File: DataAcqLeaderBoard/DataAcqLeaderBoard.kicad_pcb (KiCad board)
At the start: 2 copper layers, 1 part, among them U1 PA1616S_GPS

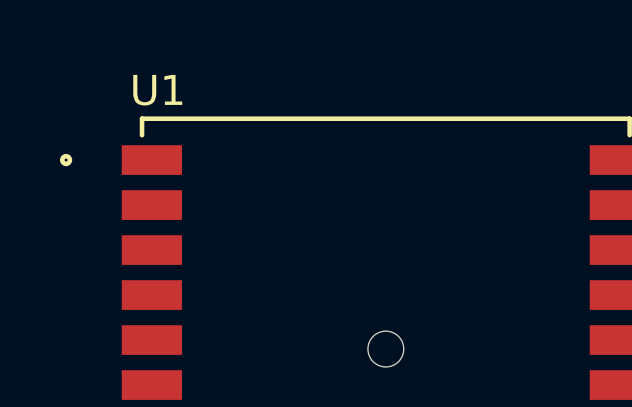
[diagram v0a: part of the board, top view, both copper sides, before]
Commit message: Removed old junk (symbol, footprint file setup)
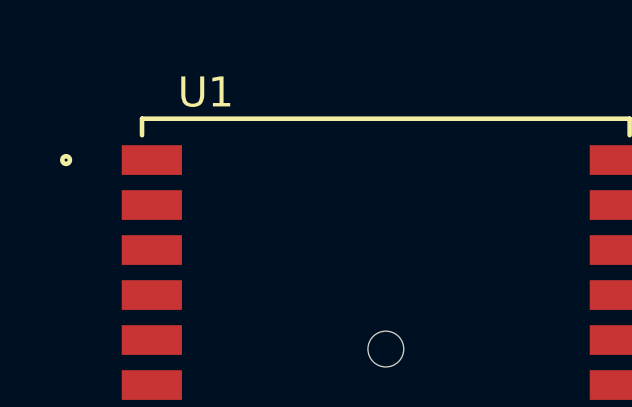
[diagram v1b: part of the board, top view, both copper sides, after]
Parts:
- U1: footprint PA_1616S_GPS:PA1616S_ADA -> DataAcqLeaderBoard-Footprints:PA1616S_ADA
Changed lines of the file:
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@@
 	(net 16 "/GPS_CoinBattery_Supply")
 	(net 17 "/GPS_NReset")
-	(footprint "PA_1616S_GPS:PA1616S_ADA"
+	(footprint "DataAcqLeaderBoard-Footprints:PA1616S_ADA"
 		(layer "F.Cu")
 		(at 175.8 93.15)
 		(tags "790 ")
 		(property "Reference" "U1"
-			(at -7.6 -9.05 0)
+			(at -6 -9 0)
 			(unlocked yes)
 			(layer "F.SilkS")
@@
 		)
 		(property "Value" "PA1616S_GPS"
-			(at 0 -5.95 0)
+			(at 0 -11 0)
 			(unlocked yes)
 			(layer "F.Fab")
@@
 			)
 		)
-		(property "Footprint" "PA_1616S_GPS:PA1616S_ADA"
+		(property "Footprint" "DataAcqLeaderBoard-Footprints:PA1616S_ADA"
 			(at 0 0 0)
 			(unlocked yes)
@@
 		)
 		(fp_text user "${REFERENCE}"
-			(at -7.6 -9.05 0)
-			(unlocked yes)
-			(layer "F.Fab")
+			(at 0 -0.5 0)
+			(unlocked yes)
+			(layer "F.Fab")

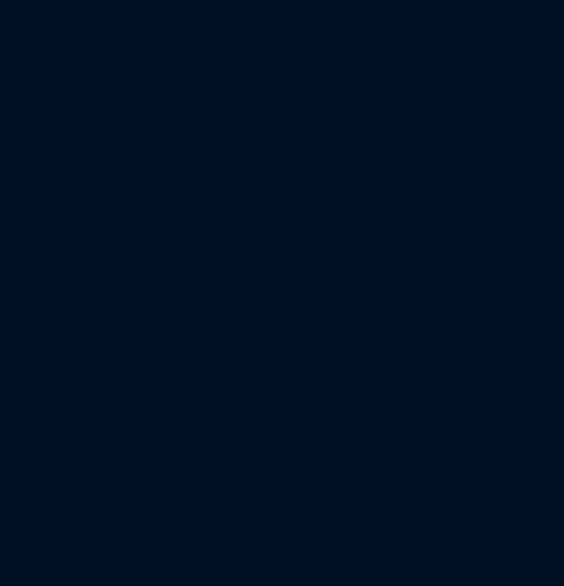
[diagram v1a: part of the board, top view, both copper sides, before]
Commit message: Added Digi XBee LTE Module
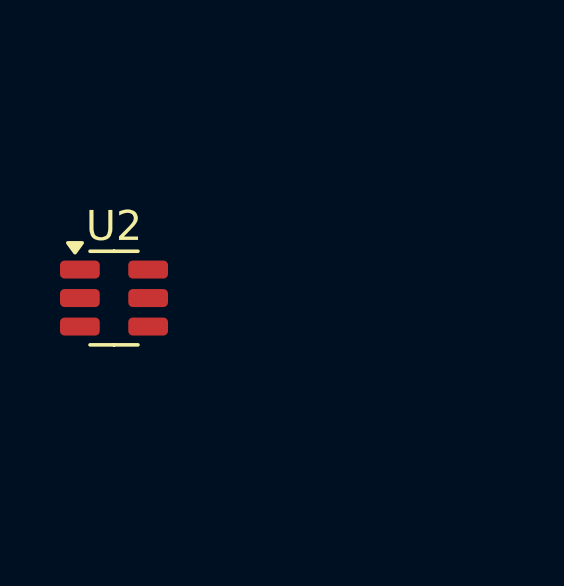
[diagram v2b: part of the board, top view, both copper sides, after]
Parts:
- added U2: USBLC6-2SC6, Package_TO_SOT_SMD:SOT-23-6, F.Cu at (147.0, 91.0)

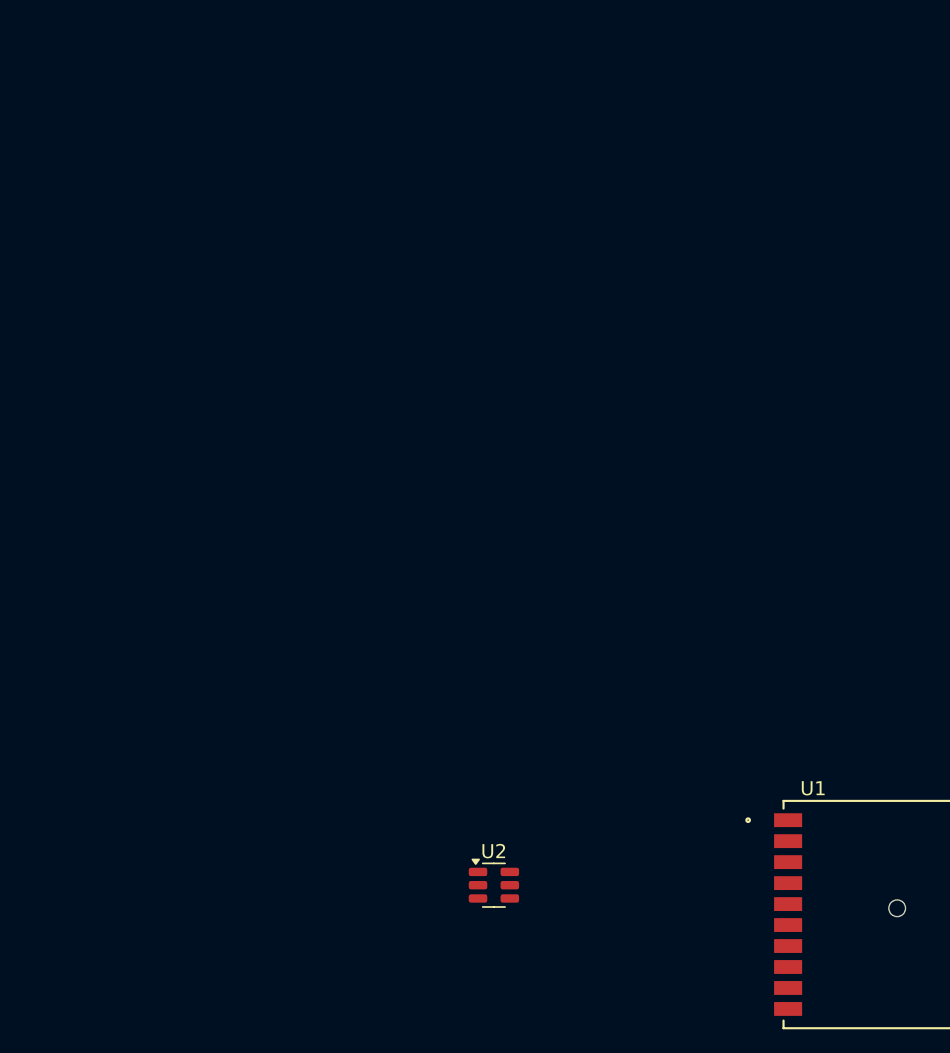
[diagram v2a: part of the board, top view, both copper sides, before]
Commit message: Added XBee RF and LTE Footprints
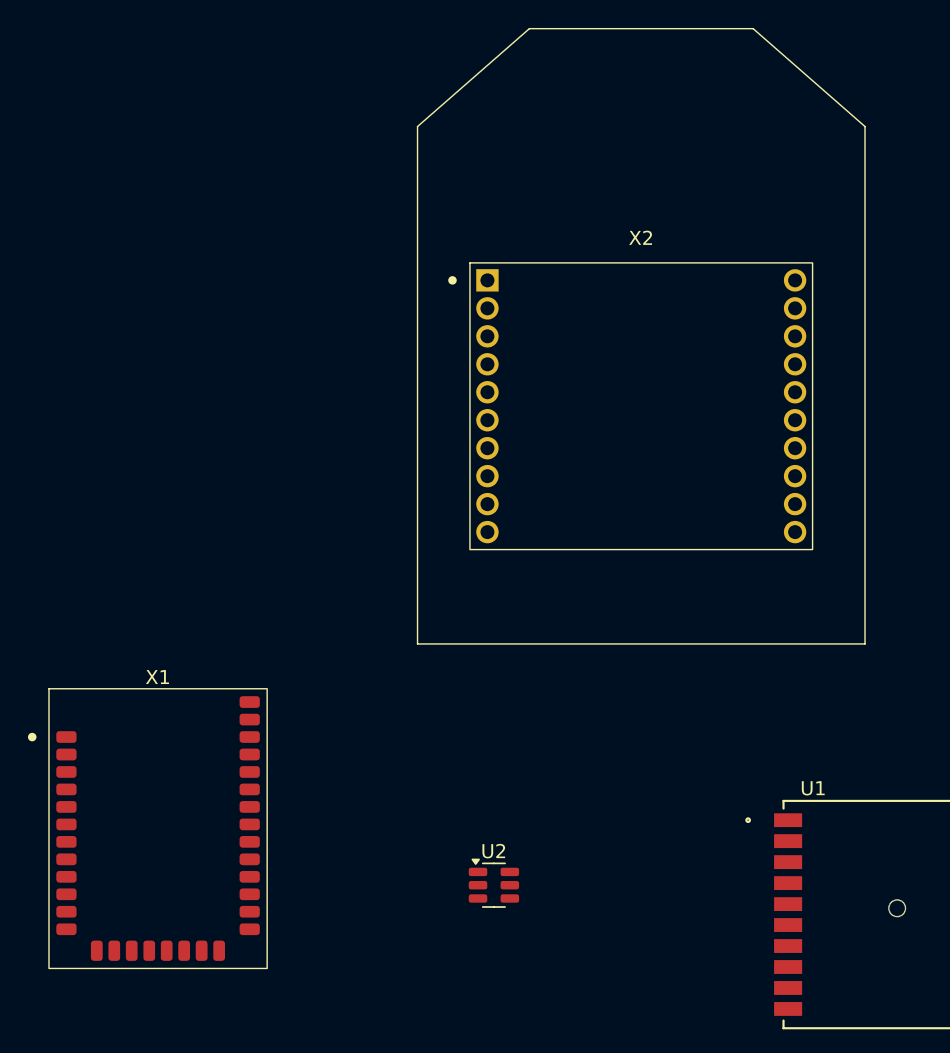
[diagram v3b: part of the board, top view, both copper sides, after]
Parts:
- added X1: DigiXBeeRX900Micro, DataAcqLeaderBoard-Footprints:XBeeXR900RFMicro, F.Cu at (122.9, 87.0)
- added X2: DigiXBee3LTECat4, DataAcqLeaderBoard-Footprints:DigiXBee3LTECat4, F.Cu at (157.5, 55.8)
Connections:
- net /GPS_1PPS_ToMCU renamed /GPS_1PPS
- net /GPS_NReset renamed /GPS_NRESET
- net Net-(U1-VCC) renamed /GPS_VCC
- U1 pad 10: /GPS_UART_RX -> unconnected-(U1-RX0-Pad10)
- U1 pad 14: unconnected-(U1-RTCM(I2C_SCL)-Pad14) -> /GPS_I2C_SCL
- U1 pad 15: unconnected-(U1-TX1(I2C_SDA)-Pad15) -> /GPS_I2C_SDA
- U1 pad 9: /GPS_UART_TX -> unconnected-(U1-TX0-Pad9)
- U2 pad 1: Net-(J2-D--PadA7) -> /USBC_D-
- U2 pad 3: Net-(J2-D+-PadA6) -> /USBC_D-

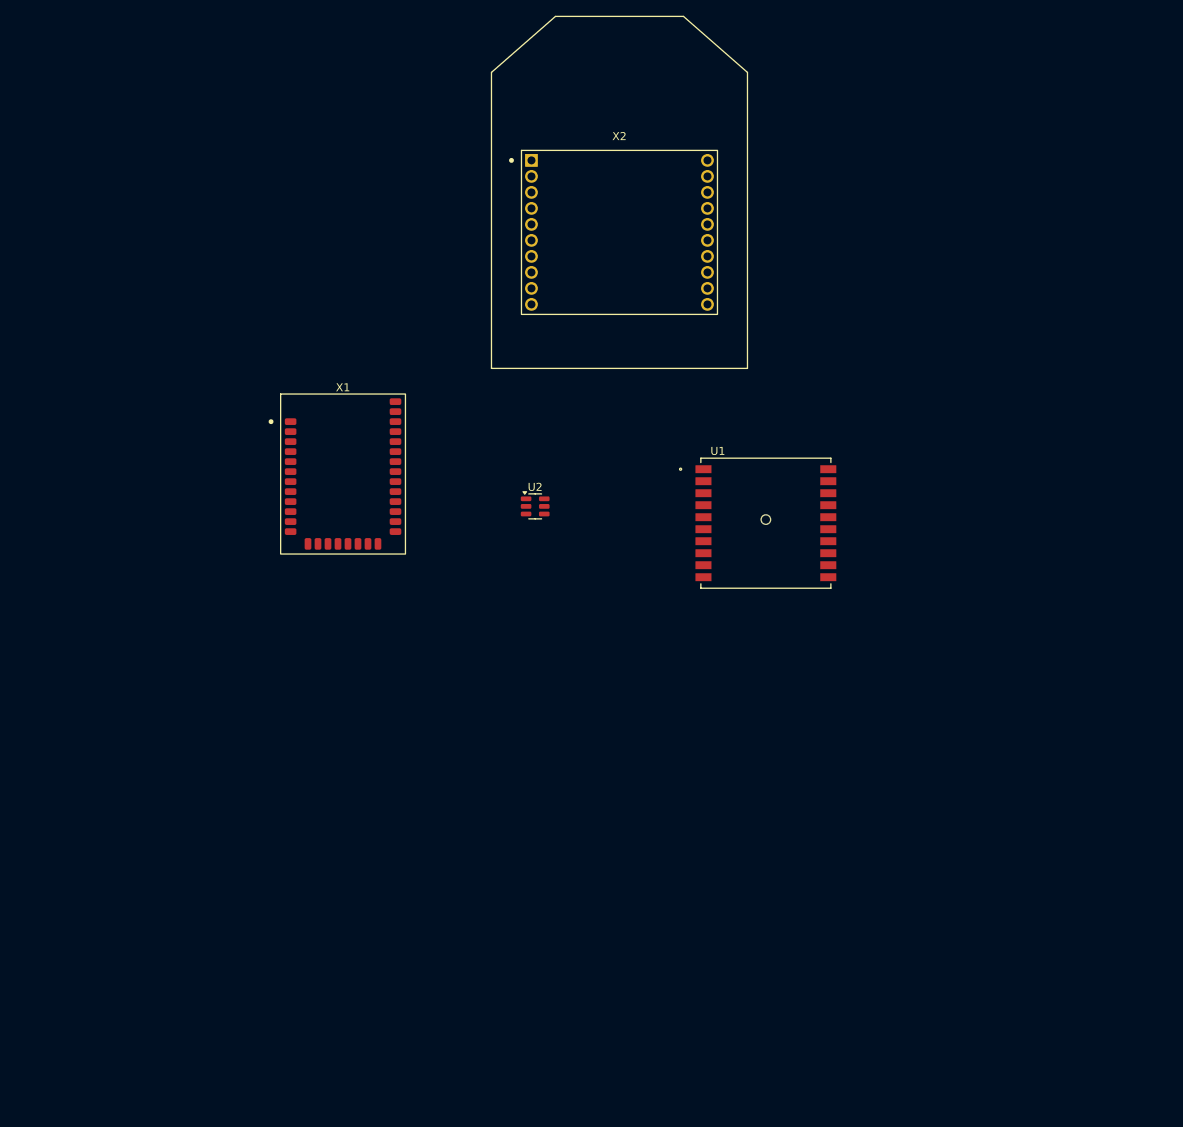
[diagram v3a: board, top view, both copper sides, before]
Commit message: Interfaced Leader SOM and added UTSVT Library
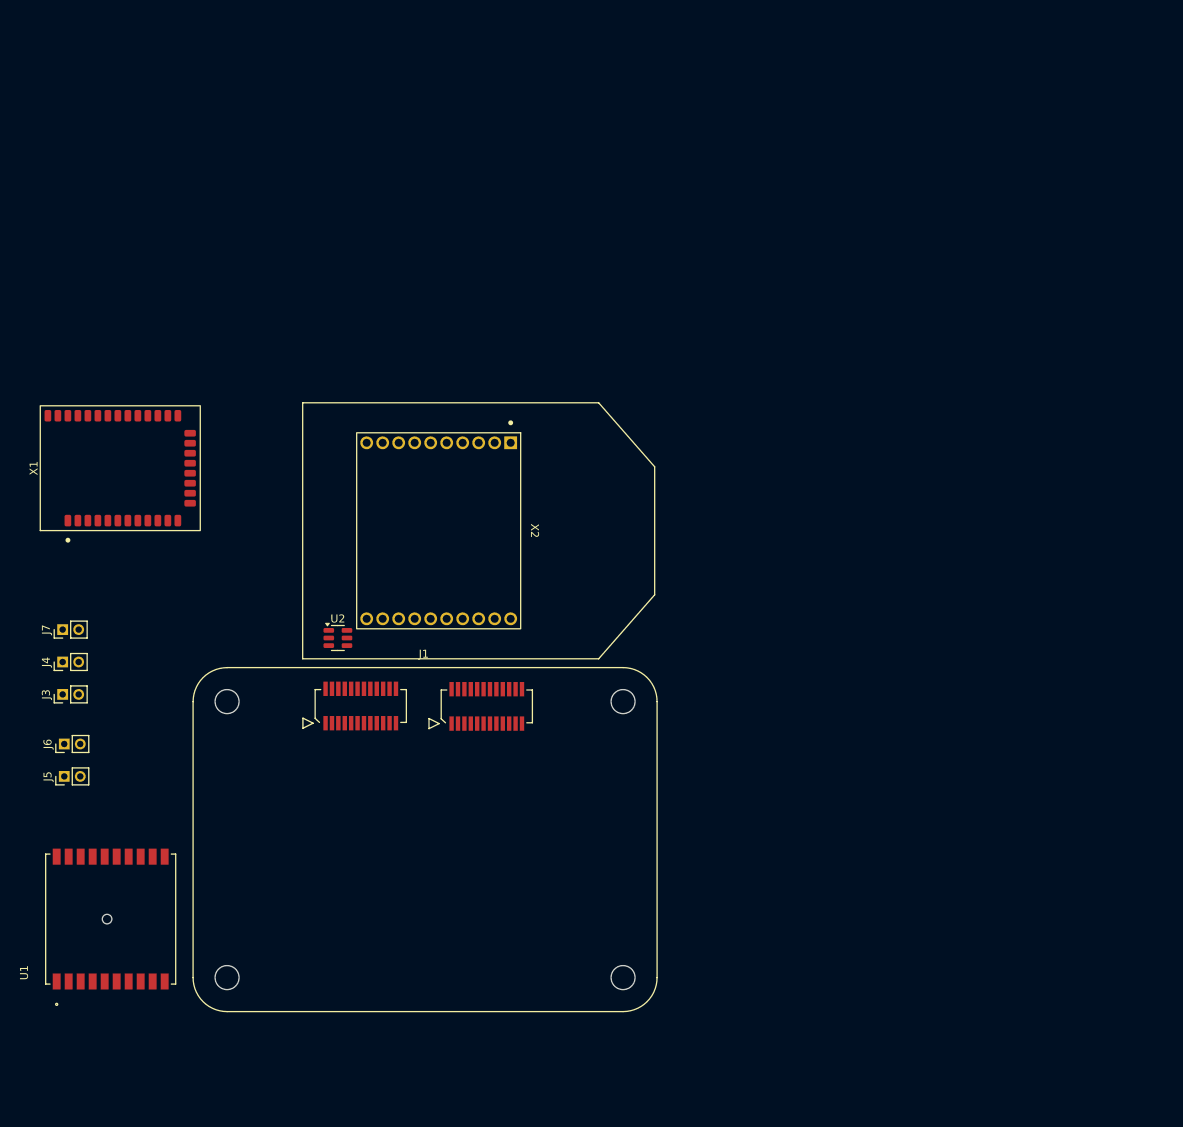
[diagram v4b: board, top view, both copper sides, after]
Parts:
- added J1: ~, UTSVT_Special:LeaderSOM, F.Cu at (133.0, 110.0)
- added J3: Conn_01x02, Connector_PinHeader_2.00mm:PinHeader_1x02_P2.00mm_Vertical, F.Cu at (87.9, 114.5)
- added J4: Conn_01x02, Connector_PinHeader_2.00mm:PinHeader_1x02_P2.00mm_Vertical, F.Cu at (87.9, 110.5)
- added J5: Conn_01x02, Connector_PinHeader_2.00mm:PinHeader_1x02_P2.00mm_Vertical, F.Cu at (88.1, 124.8)
- added J6: Conn_01x02, Connector_PinHeader_2.00mm:PinHeader_1x02_P2.00mm_Vertical, F.Cu at (88.1, 120.8)
- added J7: Conn_01x02, Connector_PinHeader_2.00mm:PinHeader_1x02_P2.00mm_Vertical, F.Cu at (87.9, 106.5)
- moved U1 95.7 mm to (93.9, 142.6), turned to 90 degrees
- moved X2 44.0 mm to (135.9, 94.1), turned to -90 degrees
- moved U2 29.6 mm to (122.3, 107.5)
- moved X1 27.9 mm to (95.1, 86.3), turned to 90 degrees
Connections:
- net /GPS_3D_Fix_ToMCU renamed /GPS_3D_Fix
- U1 pad 13: /GPS_1PPS -> unconnected-(U1-1PPS-Pad13)
- X1 pad 20: /RF_COMISSION -> unconnected-(X1-COMMISSION/[reserved]-Pad20)
- X1 pad 3: Net-(X1-UART_TX/DIO13) -> /RF_UART_TX
- X1 pad 4: Net-(X1-UART_RX/N_CONFIG/DIO14) -> /RF_UART_RX
- X2 pad 2: Net-(X2-UART_TX) -> /LTE_UART_TX
- X2 pad 3: Net-(X2-UART_RX/N_CONFIG) -> /LTE_UART_RX

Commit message: First revision of schematic done
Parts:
- removed U2: USBLC6-2SC6, Package_TO_SOT_SMD:SOT-23-6
- added BAT1: ML414, DataAcqLeaderBoard-Footprints:BAT_2994TR, F.Cu at (112.0, 150.0)
- added C1: 10u, Capacitor_SMD:C_0805_2012Metric, F.Cu at (125.7, 133.8)
- added C10: 10n, Capacitor_SMD:C_0805_2012Metric, F.Cu at (131.7, 138.2)
- added C11: 56p, Capacitor_SMD:C_0805_2012Metric, F.Cu at (128.7, 138.2)
- added C12: 10p, Capacitor_SMD:C_0805_2012Metric, F.Cu at (125.7, 138.2)
- added C13: 10n, Capacitor_SMD:C_0805_2012Metric, F.Cu at (122.7, 138.2)
- added C14: 1u, Capacitor_SMD:C_0805_2012Metric, F.Cu at (134.7, 142.7)
- added C15: 1u, Capacitor_SMD:C_0805_2012Metric, F.Cu at (134.7, 133.8)
- added C16: 0.1u, Capacitor_SMD:C_0805_2012Metric, F.Cu at (131.7, 133.8)
- added C17: 1u, Capacitor_SMD:C_0805_2012Metric, F.Cu at (119.6, 138.2)
- added C18: 1u, Capacitor_SMD:C_0805_2012Metric, F.Cu at (124.2, 143.1)
- added C19: 0.1u, Capacitor_SMD:C_0805_2012Metric, F.Cu at (128.7, 133.8)
- added C2: 1u, Capacitor_SMD:C_0805_2012Metric, F.Cu at (122.7, 133.8)
- added C3: 47p, Capacitor_SMD:C_0805_2012Metric, F.Cu at (119.6, 133.8)
- added C4: 1u, Capacitor_SMD:C_0805_2012Metric, F.Cu at (128.7, 142.7)
- added C5: 1u, Capacitor_SMD:C_0805_2012Metric, F.Cu at (131.7, 142.7)
- added C6: 100u, Capacitor_SMD:C_0805_2012Metric, F.Cu at (133.3, 152.5)
- added C7: 100u, Capacitor_SMD:C_0805_2012Metric, F.Cu at (133.3, 148.2)
- added C8: 100u, Capacitor_SMD:C_0805_2012Metric, F.Cu at (128.0, 156.0)
- added C9: 10u, Capacitor_SMD:C_0805_2012Metric, F.Cu at (134.7, 138.2)
- added D1: RF_COM, LED_SMD:LED_0805_2012Metric, F.Cu at (115.0, 103.0)
- added D2: RF_MOD, LED_SMD:LED_0805_2012Metric, F.Cu at (103.0, 103.0)
- added D3: RF_ON, LED_SMD:LED_0805_2012Metric, F.Cu at (97.0, 103.0)
- added D4: RF_RSSI, LED_SMD:LED_0805_2012Metric, F.Cu at (109.0, 103.0)
- added D5: LTE_CONN, LED_SMD:LED_0805_2012Metric, F.Cu at (160.0, 101.0)
- added D6: LTE_RSSI, LED_SMD:LED_0805_2012Metric, F.Cu at (160.0, 107.0)
- added D7: LTE_ON, LED_SMD:LED_0805_2012Metric, F.Cu at (160.0, 113.0)
- added D8: !3D_FX, LED_SMD:LED_0805_2012Metric, F.Cu at (102.9, 134.0)
- added FB1: FerriteBead, Resistor_SMD:R_0402_1005Metric, F.Cu at (153.9, 125.0)
- added H1: M.3, MountingHole:MountingHole_3mm, F.Cu at (90.0, 80.0)
- added H2: M.3, MountingHole:MountingHole_3mm, F.Cu at (160.0, 80.0)
- added H3: M.3, MountingHole:MountingHole_3mm, F.Cu at (90.0, 160.0)
- added R1: 10k, Resistor_SMD:R_0805_2012Metric, F.Cu at (152.4, 142.6)
- added R10: 700, Resistor_SMD:R_0805_2012Metric, F.Cu at (140.9, 161.1)
- added R11: 700, Resistor_SMD:R_0805_2012Metric, F.Cu at (143.9, 161.1)
- added R12: 700, Resistor_SMD:R_0805_2012Metric, F.Cu at (146.8, 161.1)
- added R13: 10k, Resistor_SMD:R_0805_2012Metric, F.Cu at (157.4, 134.4)
- added R14: 10k, Resistor_SMD:R_0805_2012Metric, F.Cu at (157.4, 137.4)
- added R15: 10k, Resistor_SMD:R_0805_2012Metric, F.Cu at (149.5, 142.6)
- added R16: 700, Resistor_SMD:R_0805_2012Metric, F.Cu at (146.5, 147.0)
- added R17: 700, Resistor_SMD:R_0805_2012Metric, F.Cu at (149.8, 161.1)
- added R18: 10k, Resistor_SMD:R_0805_2012Metric, F.Cu at (152.4, 133.7)
- added R19: 700, Resistor_SMD:R_0805_2012Metric, F.Cu at (149.5, 147.0)
- added R2: 10k, Resistor_SMD:R_0805_2012Metric, F.Cu at (152.4, 138.1)
- added R20: 700, Resistor_SMD:R_0805_2012Metric, F.Cu at (152.8, 161.1)
- added R3: 10k, Resistor_SMD:R_0805_2012Metric, F.Cu at (140.6, 133.7)
- added R4: 700, Resistor_SMD:R_0805_2012Metric, F.Cu at (137.7, 133.7)
- added R5: 10k, Resistor_SMD:R_0805_2012Metric, F.Cu at (149.5, 138.1)
- added R6: 700, Resistor_SMD:R_0805_2012Metric, F.Cu at (143.6, 147.0)
- added R7: 700, Resistor_SMD:R_0805_2012Metric, F.Cu at (132.1, 161.1)
- added R8: 700, Resistor_SMD:R_0805_2012Metric, F.Cu at (135.1, 161.1)
- added R9: 700, Resistor_SMD:R_0805_2012Metric, F.Cu at (138.0, 161.1)
- added SW1: RF_RESET, Button_Switch_SMD:SW_SPST_B3SL-1002P, F.Cu at (118.0, 81.0)
- added SW2: RF_COM, Button_Switch_SMD:SW_SPST_B3SL-1002P, F.Cu at (118.1, 92.0)
- added SW3: LTE_RESET, Button_Switch_SMD:SW_SPST_B3SL-1002P, F.Cu at (160.0, 92.0)
- added SW4: GPS_RESET, Button_Switch_SMD:SW_SPST_B3SL-1002P, F.Cu at (100.0, 161.0)
- added TP1: RF_UART_RX, UTSVT_Special:TestPoint_HEX_3mmID, F.Cu at (144.0, 154.0)
- added TP2: RF_UART_TX, UTSVT_Special:TestPoint_HEX_3mmID, F.Cu at (148.0, 154.0)
- added TP3: RF_NREST, UTSVT_Special:TestPoint_HEX_3mmID, F.Cu at (160.0, 154.0)
- added TP4: LTE_UART_TX, UTSVT_Special:TestPoint_HEX_3mmID, F.Cu at (152.0, 154.0)
- added TP5: LTE_UART_RX, UTSVT_Special:TestPoint_HEX_3mmID, F.Cu at (140.0, 154.0)
- added TP6: LTE_NRESET, UTSVT_Special:TestPoint_HEX_3mmID, F.Cu at (156.0, 154.0)
- J2: renamed from J3; value Conn_01x02 -> PER_CAN
- J3: renamed from J4; value Conn_01x02 -> PER_PWR
- J4: renamed from J5; value Conn_01x02 -> CCAN_IN
- J5: renamed from J6; value Conn_01x02 -> CCAN_OUT
- J6: renamed from J7; value Conn_01x02 -> PWR_IN
- moved J6 11.7 mm to (90.0, 118.0), turned to 0 degrees
- moved J5 11.4 mm to (90.0, 132.0), turned to 0 degrees
- moved J2 10.8 mm to (90.0, 104.0), turned to 0 degrees
- moved J1 10.3 mm to (135.1, 120.1)
- moved X1 7.93 mm to (103.0, 87.0), turned to 0 degrees
- moved X2 5.43 mm to (140.0, 97.7), turned to 0 degrees
- moved U1 4.51 mm to (96.1, 146.6), turned to 180 degrees
- moved J3 2.16 mm to (90.0, 111.0), turned to 0 degrees
- moved J4 1.91 mm to (90.0, 125.0), turned to 0 degrees
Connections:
- X2 pad 7: /LTE_USB_D+ -> Net-(X2-PWM1/DIO11/USB_D+/I2C_SDA)
- X2 pad 8: /LTE_USB_D- -> Net-(X2-USB_D-)
